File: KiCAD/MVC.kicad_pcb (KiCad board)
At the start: 2 copper layers, 100 x 100 mm, 28 parts, among them J1 FBank Switch, J2 Conn_02x02_Odd_Even, J3 Conn_01x22_Female, J4 Conn_02x23_Odd_Even, SW1 reset, U1 74HC00, U2 6502, U3 28C256, U4 62256, U5 6522, U6 74HC00, U7 74LS30, X1 CXO_DIP14

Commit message: Built first ugly mainboard
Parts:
- added REF**: DIP-28_W7.62mm_LongPads, Package_DIP:DIP-28_W7.62mm_LongPads, F.Cu at (144.1, 60.7)
- added REF**: MountingHole_4.3mm_M4, MountingHole:MountingHole_4.3mm_M4, F.Cu at (54.0, 145.0)
- added REF**: MountingHole_4.3mm_M4, MountingHole:MountingHole_4.3mm_M4, F.Cu at (54.0, 55.0)
- added REF**: MountingHole_4.3mm_M4, MountingHole:MountingHole_4.3mm_M4, F.Cu at (185.0, 145.0)
- added REF**: MountingHole_4.3mm_M4, MountingHole:MountingHole_4.3mm_M4, F.Cu at (185.0, 55.0)
- moved D1 120.7 mm to (160.0, 128.3)
- moved U1 117.7 mm to (151.8, 76.5), turned to 90 degrees
- moved C3 98.8 mm to (140.1, 129.2)
- moved D4 96.4 mm to (160.0, 147.3)
- moved R2 93.1 mm to (172.9, 68.9), turned to 270 degrees
- moved D2 92.5 mm to (160.0, 134.6)
- moved U2 92.1 mm to (111.4, 131.4), turned to 180 degrees
- moved C8 91.4 mm to (102.6, 77.4)
- moved J4 87.2 mm to (129.3, 52.0), turned to 270 degrees
- moved D3 85.8 mm to (160.0, 141.0)
- moved J1 75.2 mm to (179.1, 73.7), turned to 180 degrees
- moved C7 70.9 mm to (119.1, 145.8), turned to 180 degrees
- moved C1 68.7 mm to (63.9, 53.8)
- moved U6 66.4 mm to (124.5, 146.5), turned to 90 degrees
- moved U3 65.1 mm to (169.8, 88.2)
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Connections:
- J4 pad 46: /~BE~ -> /BE
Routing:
- net /a15: track 0.00 -> 215.4 mm, vias 0 -> 7
- net /R~W~: track 0.00 -> 206.8 mm, vias 0 -> 7
- net /a13: track 0.00 -> 204.9 mm, vias 0 -> 4
- net /a0: track 0.00 -> 188.7 mm, vias 0 -> 2
- net /a10: track 0.00 -> 187.2 mm, vias 0 -> 6
- net /d5: track 0.00 -> 186.9 mm, vias 0 -> 4
- net /d4: track 0.00 -> 186.2 mm, vias 0 -> 4
- net /a11: track 0.00 -> 186.0 mm, vias 0 -> 4
- net /d7: track 0.00 -> 184.5 mm, vias 0 -> 4
- net /a1: track 0.00 -> 184.2 mm, vias 0 -> 2
- net /a12: track 0.00 -> 183.3 mm, vias 0 -> 3
- net /a9: track 0.00 -> 182.8 mm, vias 0 -> 6
- net /d6: track 0.00 -> 181.7 mm, vias 0 -> 4
- net /d3: track 0.00 -> 178.3 mm, vias 0 -> 3
- net /a14: track 0.00 -> 173.2 mm, vias 0 -> 5
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- added copper zone on B.Cu, net +5V
- added copper zone on F.Cu, net GND
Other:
- board size 100 x 100 mm -> 141 x 100 mm
- board text added: "5V"
- board text added: "5v"
- board text added: "BE"
- board text added: "CA1"
- board text added: "CA2"
- board text added: "CB1"
- board text added: "CB2"
- board text added: "Flash Bank"
- board text added: "GND"
- board text added: "J. Alex Cuoghi voltair.us 2020-10-09"
- board text added: "PA0"
- board text added: "PA1"
- board text added: "PA2"
- board text added: "PA3"
- board text added: "PA4"
- board text added: "PA5"
- board text added: "PA6"
- board text added: "PA7"
- board text added: "PB0"
- board text added: "PB1"
- board text added: "PB2"
- board text added: "PB3"
- board text added: "PB4"
- board text added: "PB5"
- board text added: "PB6"
- board text added: "PB7"
- board text added: "Protoyping"
- board text added: "gnd"
- board text added: "~NMI~"

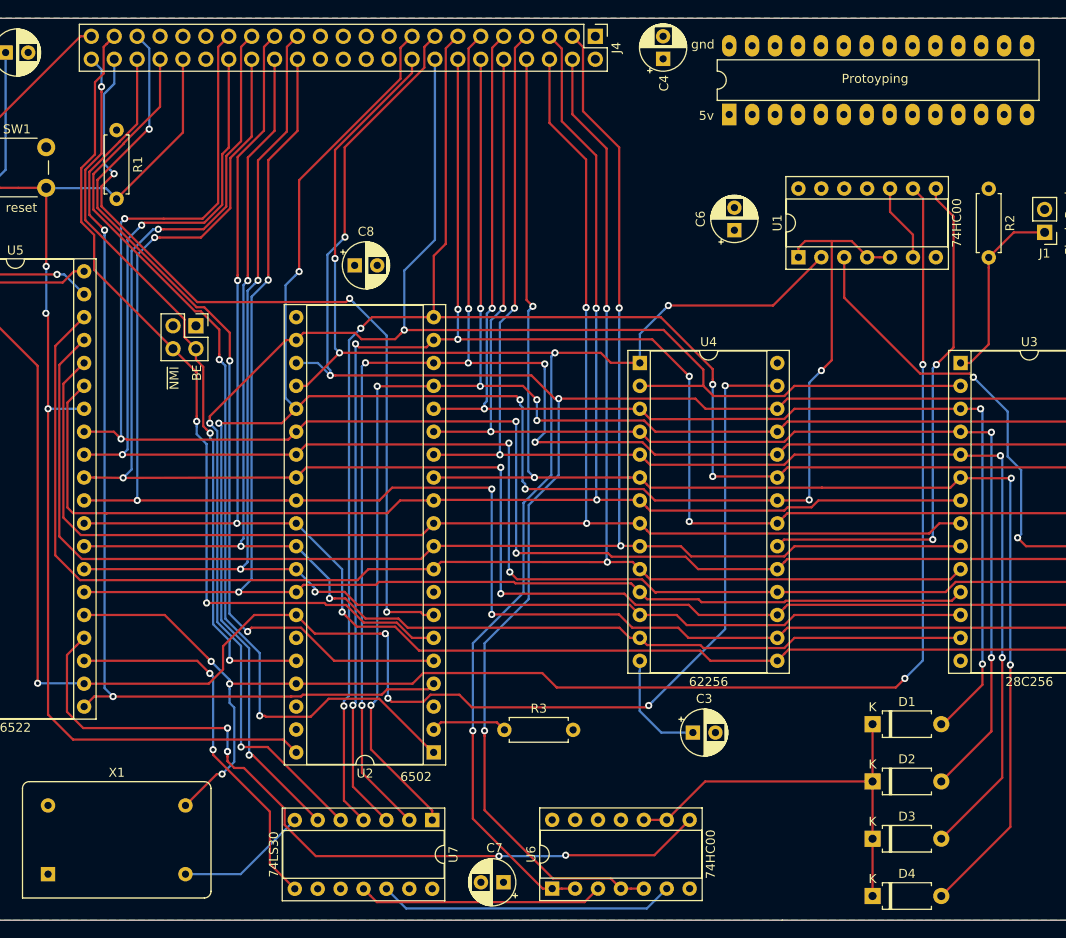
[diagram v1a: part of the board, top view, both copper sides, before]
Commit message: Fixed issues found in PCB over testing through apr
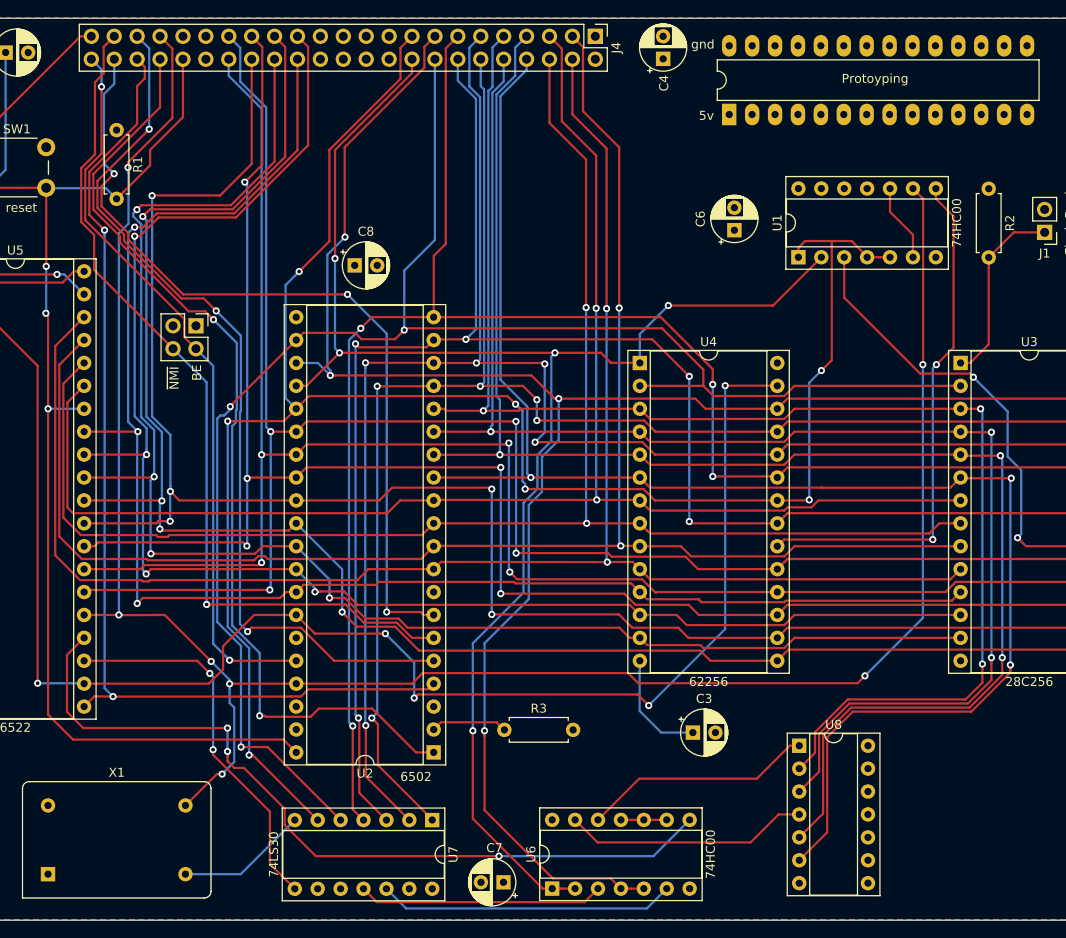
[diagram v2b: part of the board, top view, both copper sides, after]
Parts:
- removed D1, D2, D3, D4: 1N4148, Diode_THT:D_A-405_P7.62mm_Horizontal
- added U8: 74HC02, Package_DIP:DIP-14_W7.62mm_Socket, F.Cu at (151.9, 130.7)
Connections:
- U1 pad 9: /CLK -> /~CLK~
- U2 pad 37: /CLK -> /~CLK~
- U5 pad 25: /CLK -> /~CLK~
- U5 pad 26: /d0 -> /d7
- U5 pad 27: /d1 -> /d6
- U5 pad 28: /d2 -> /d5
- U5 pad 29: /d3 -> /d4
- U5 pad 30: /d4 -> /d3
- U5 pad 31: /d5 -> /d2
- U5 pad 32: /d6 -> /d1
- U5 pad 33: /d7 -> /d0
- U6 pad 10: Net-(D1-Pad1) -> Net-(U6-Pad10)
- U6 pad 11: (no net) -> Net-(U6-Pad10)
- U6 pad 12: (no net) -> Net-(U6-Pad12)
- U6 pad 13: (no net) -> Net-(U6-Pad13)
- U6 pad 9: Net-(D1-Pad1) -> Net-(U6-Pad10)
- X1 pad 8: /CLK -> /~CLK~
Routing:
- net /~CLK~: track 0.00 -> 232.0 mm, vias 0 -> 7
- net /CLK: track 167.9 -> 0.00 mm, vias 5 -> 0
- net Net-(D1-Pad1): track 45.2 -> 0.00 mm
- net Net-(U6-Pad13): track 0.00 -> 27.2 mm
- net Net-(U6-Pad12): track 0.00 -> 25.7 mm
- net /a7: track 140.8 -> 160.3 mm, vias 4 -> 3
- net /a6: track 145.7 -> 161.0 mm, vias 4 -> 3
- net /a5: track 156.8 -> 171.2 mm, vias 4 -> 3
- net /d2: track 159.1 -> 172.5 mm, vias 3 -> 4
- net /d0: track 160.8 -> 174.1 mm, vias 2 -> 3
- net /d3: track 178.3 -> 191.2 mm, vias 3 -> 4
- net /d1: track 162.2 -> 175.1 mm, vias 3 -> 4
- net /a4: track 161.7 -> 173.8 mm, vias 4 -> 3
- net /d7: track 184.5 -> 192.5 mm
- net Net-(U6-Pad10): track 0.00 -> 5.08 mm
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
